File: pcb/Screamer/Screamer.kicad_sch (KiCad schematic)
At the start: 52 parts, among them J1 Conn_01x04, SW100 SW_DPDT_x2, SW102 SW_SPDT

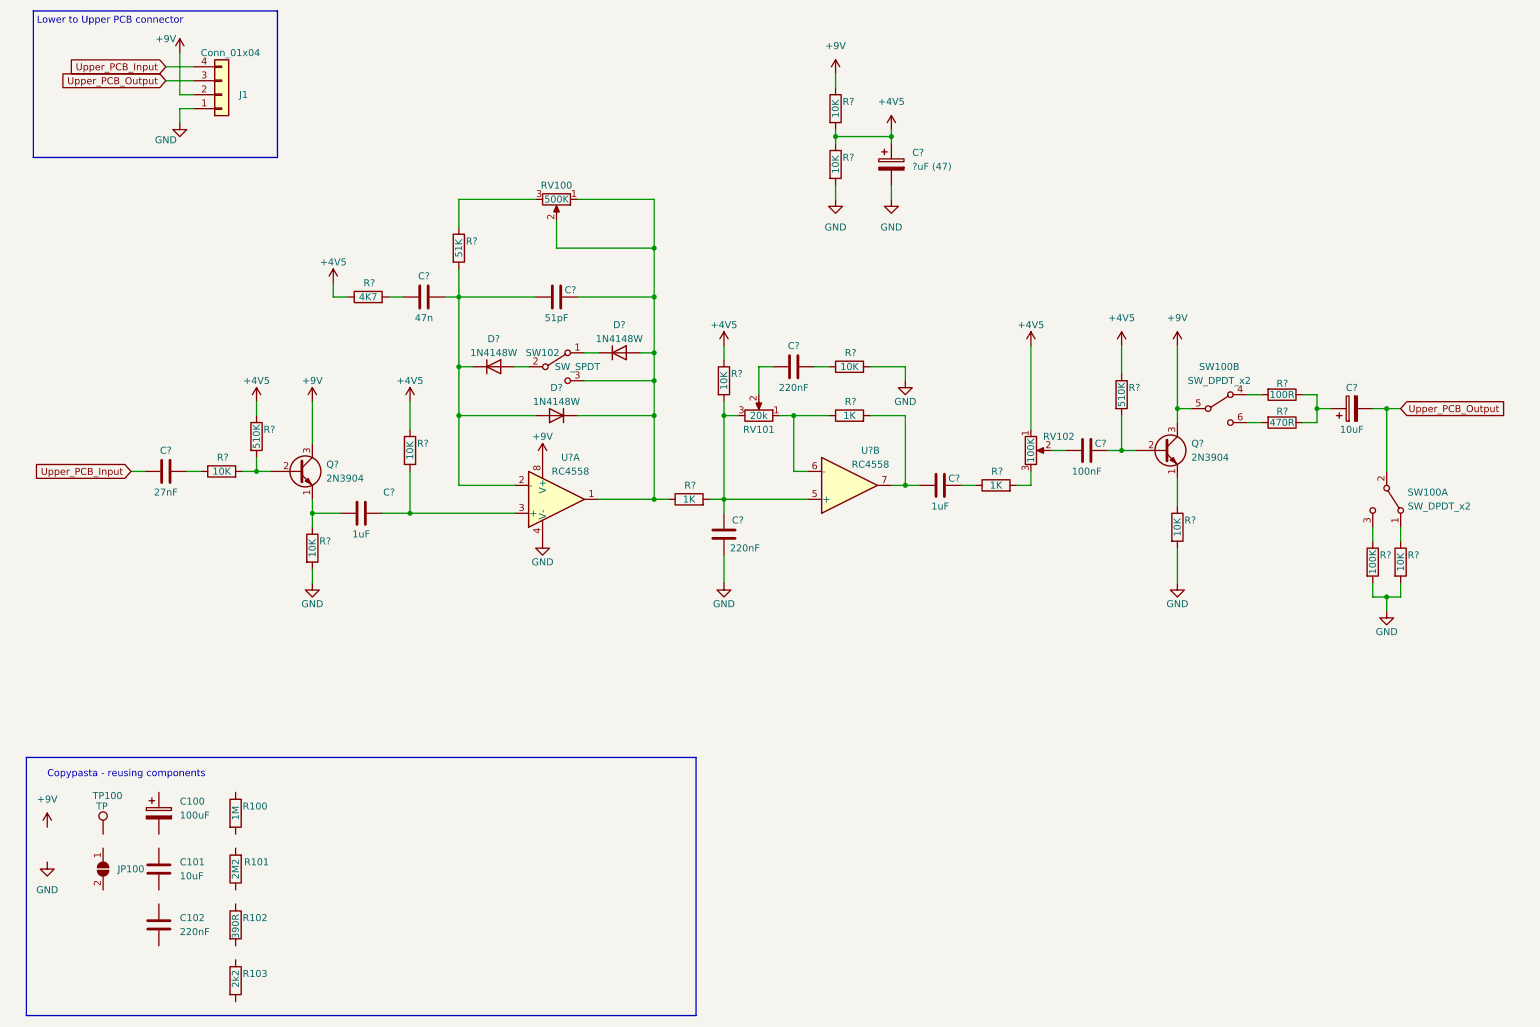
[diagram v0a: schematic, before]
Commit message: [Screamer] update schematic and assign LCSC parts
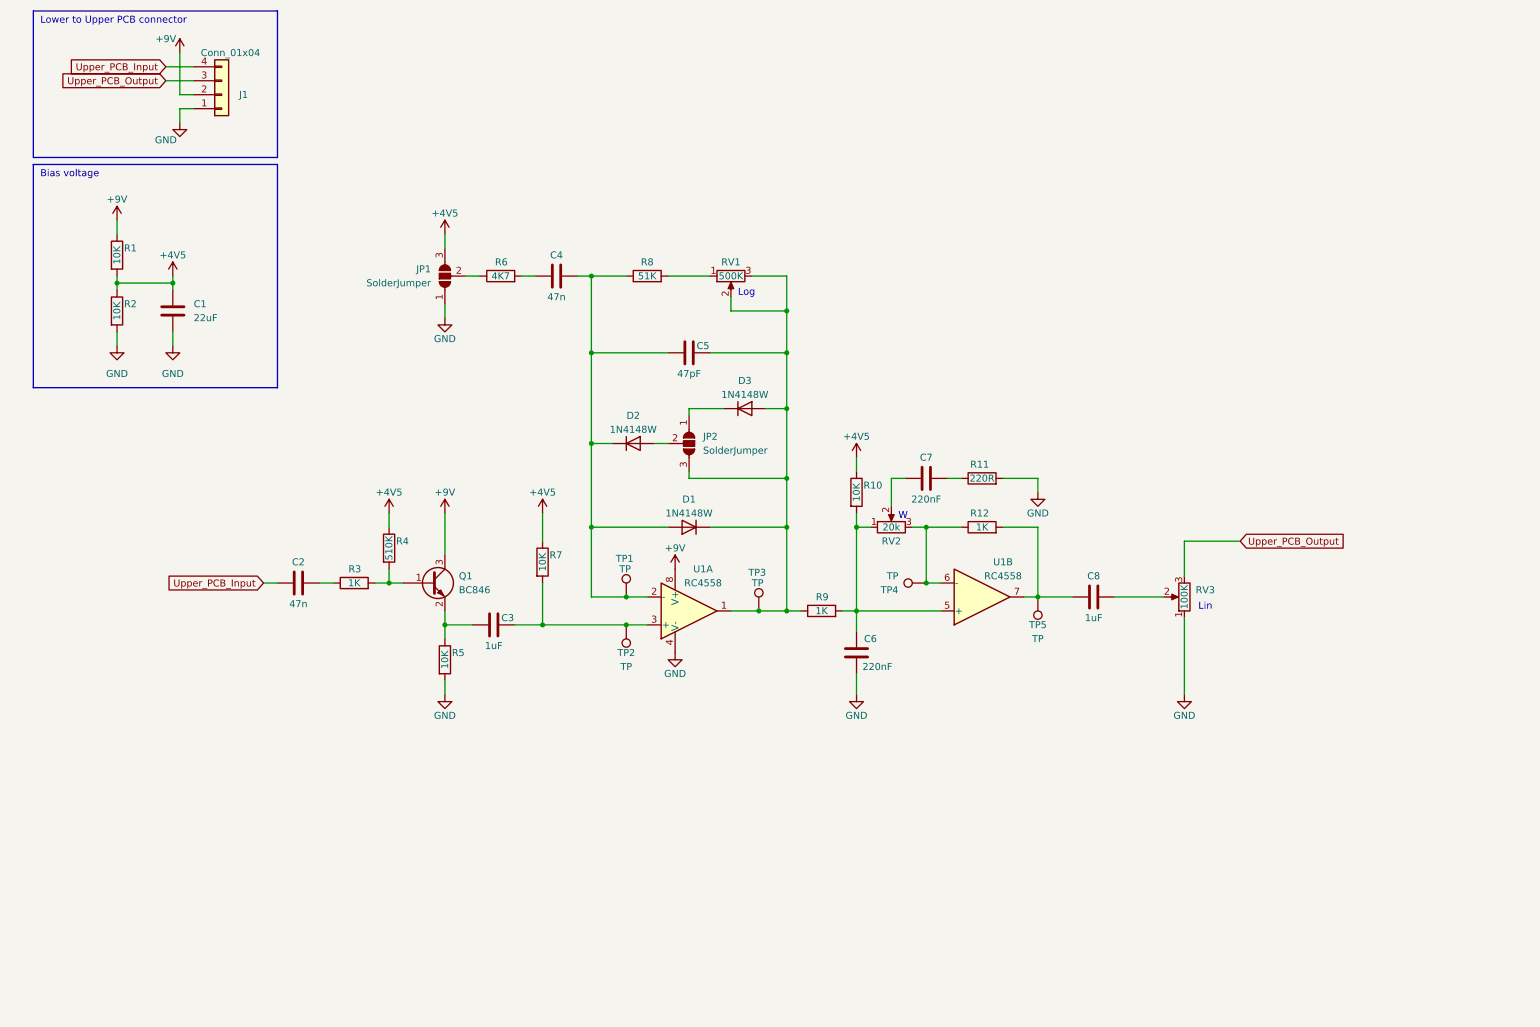
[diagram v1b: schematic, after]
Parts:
- removed C100: 100uF, Capacitor_THT:CP_Radial_D5.0mm_P2.00mm, symbol Device:C_Polarized
- removed C101: 10uF, Capacitor_SMD:C_0805_2012Metric, symbol Device:C
- removed C102: 220nF, Capacitor_SMD:C_0603_1608Metric, symbol Device:C
- removed C?: ?uF (47), symbol Device:C_Polarized
- removed C?: 10uF, symbol Device:C_Polarized
- removed C?: 100nF, symbol Device:C
- removed C?: 27nF, symbol Device:C
- removed JP100: Jmp, Jumper:SolderJumper-2_P1.3mm_Open_TrianglePad1.0x1.5mm, symbol Jumper:SolderJumper_2_Open
- removed Q? (x2): 2N3904, Package_TO_SOT_THT:TO-92_Inline, symbol Transistor_BJT:2N3904
- removed R100: 1M, Resistor_SMD:R_0603_1608Metric, symbol Device:R
- removed R101: 2M2, Resistor_SMD:R_0603_1608Metric, symbol Device:R
- removed R102: 390R, Resistor_SMD:R_0603_1608Metric, symbol Device:R
- removed R103: 2k2, Resistor_SMD:R_0603_1608Metric, symbol Device:R
- removed R?: 100K, Resistor_SMD:R_0603_1608Metric, symbol Device:R
- removed R? (x2): 10K, Resistor_SMD:R_0603_1608Metric, symbol Device:R
- removed R?: 510K, Resistor_SMD:R_0603_1608Metric, symbol Device:R
- removed R?: 470R, Resistor_SMD:R_0603_1608Metric, symbol Device:R
- removed R?: 1K, Resistor_SMD:R_0603_1608Metric, symbol Device:R
- removed R?: 100R, Resistor_SMD:R_0603_1608Metric, symbol Device:R
- removed SW100: SW_DPDT_x2, MeineBib:Switch_toggle_DPDT_Print, symbol Switch:SW_DPDT_x2
- removed SW102: SW_SPDT, MeineBib:Switch_toggle_SPDT_Print, symbol Switch:SW_SPDT
- removed TP100: TP, TestPoint:TestPoint_Pad_D2.0mm, symbol Connector:TestPoint
- added C1: 22uF, Capacitor_SMD:C_1206_3216Metric, symbol Device:C
- added C2: 47n, Capacitor_SMD:C_0603_1608Metric, symbol Device:C
- added JP1, JP2: SolderJumper, Jumper:SolderJumper-3_P1.3mm_Open_RoundedPad1.0x1.5mm_NumberLabels, symbol Jumper:SolderJumper_3_Open
- added Q1: BC846, Package_TO_SOT_SMD:SOT-23, symbol Transistor_BJT:BC846
- added TP1, TP2, TP3, TP4, TP5: TP, TestPoint:TestPoint_Pad_D2.0mm, symbol Connector:TestPoint
- C3, C8: renamed from C?; footprint (none) -> Capacitor_SMD:C_0603_1608Metric; LCSC C15850 -> C15849
- C4: renamed from C?; footprint (none) -> Capacitor_SMD:C_0603_1608Metric; LCSC C15850 -> C1622
- C5: renamed from C?; value 51pF -> 47pF; footprint (none) -> Capacitor_SMD:C_0603_1608Metric; LCSC C15850 -> C1671
- C6, C7: renamed from C?; footprint (none) -> Capacitor_SMD:C_0603_1608Metric; LCSC C15850 -> C21120
- R1, R10, R2, R5, R7: renamed from R?; LCSC (none) -> C25804
- R11: renamed from R?; value 10K -> 220R; LCSC (none) -> C22962
- R12, R9: renamed from R?; LCSC (none) -> C21190
- R3: renamed from R?; value 10K -> 1K; LCSC (none) -> C21190
- R4: renamed from R?; LCSC (none) -> C23192
- R6: renamed from R?; LCSC (none) -> C23162
- R8: renamed from R?; LCSC (none) -> C23196
- U1: renamed from U?; footprint (none) -> Package_SO:SO-8_3.9x4.9mm_P1.27mm; LCSC (none) -> C406864
- gave numbers to parts that had none: 3
- renumbered RV100 to RV1, RV101 to RV2, RV102 to RV3
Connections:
- net +9V: now also C1.1, JP1.3 (B), Q1.3 (C); no longer R6.1, RV3.1
- net GND: now also RV3.1, C1.2, JP1.1 (A)
- net Upper_PCB_Input: now also C2.1
- net Upper_PCB_Output: now also RV3.3
- net at C5.2, D1.1 (K), D3.2 (A)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: now also RV1.3, JP2.3 (B), TP3.1; no longer RV1.1
- net at C5.1, D1.2 (A), D2.1 (K)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: now also C4.1, R8.1, TP1.1; no longer C4.2, R8.2
- net at C3.1, R5.1: now also Q1.2 (E)
- net at R3.2, R4.2: now also Q1.1 (B)
- net at D3.1 (K): now also JP2.1 (A)
- net at D2.2 (A): now also JP2.2 (C)
- net at C6.1, R10.2, R9.2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: now also RV2.1; no longer RV2.3
- net at R6.2: now also C4.2; no longer C4.1
- net at C3.2, R7.2, U1.3 (+): now also TP2.1
- net at R3.1: now also C2.2
- net at R12.1, U1.6 (-): now also RV2.3, TP4.1; no longer RV2.1
- net at C8.1, R12.2, U1.7: now also TP5.1
- net at C8.2: now also RV3.2
- new net: R8.2, RV1.1
- new net: JP1.2 (C), R6.1
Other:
- note added: "Bias voltage"
- note added: "Lin"
- note added: "Log"
- note added: "W"
- note removed: "Copypasta - reusing components"
- moved on the sheet: C3, C4, C5, C6, C7, C8, D1, D2, D3, R1, R10, R11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

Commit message: [Screamer] Update diode footprint and start arranging stuff on PCB
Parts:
- D1, D2, D3: footprint Diode_SMD:D_SOD-123 -> MeineBib:D_SOD-123+THT
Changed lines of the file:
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@@
     (property "Reference" "D1" (id 0) (at 133.35 102.87 0))
     (property "Value" "1N4148W" (id 1) (at 133.35 105.41 0))
-    (property "Footprint" "Diode_SMD:D_SOD-123" (id 2) (at 133.35 103.505 0)
+    (property "Footprint" "MeineBib:D_SOD-123+THT" (id 2) (at 133.35 103.505 0)
       (effects (font (size 1.27 1.27)) hide)
     )
@@
     (property "Reference" "D3" (id 0) (at 143.51 81.28 0))
     (property "Value" "1N4148W" (id 1) (at 143.51 83.82 0))
-    (property "Footprint" "Diode_SMD:D_SOD-123" (id 2) (at 143.51 90.805 0)
+    (property "Footprint" "MeineBib:D_SOD-123+THT" (id 2) (at 143.51 90.805 0)
       (effects (font (size 1.27 1.27)) hide)
     )
@@
     (property "Reference" "D2" (id 0) (at 123.19 87.63 0))
     (property "Value" "1N4148W" (id 1) (at 123.19 90.17 0))
-    (property "Footprint" "Diode_SMD:D_SOD-123" (id 2) (at 123.19 97.155 0)
+    (property "Footprint" "MeineBib:D_SOD-123+THT" (id 2) (at 123.19 97.155 0)
       (effects (font (size 1.27 1.27)) hide)
     )
@@
     )
     (path "/06bd8af6-5f31-48d1-8dfe-e47bb2fbf937"
-      (reference "D1") (unit 1) (value "1N4148W") (footprint "Diode_SMD:D_SOD-123")
+      (reference "D1") (unit 1) (value "1N4148W") (footprint "MeineBib:D_SOD-123+THT")
     )
     (path "/8885a9d9-16dd-4476-9879-de777ac2f14c"
-      (reference "D2") (unit 1) (value "1N4148W") (footprint "Diode_SMD:D_SOD-123")
+      (reference "D2") (unit 1) (value "1N4148W") (footprint "MeineBib:D_SOD-123+THT")
     )
     (path "/2b9560aa-ca85-40bd-96c0-e06c0c8c5ac1"
-      (reference "D3") (unit 1) (value "1N4148W") (footprint "Diode_SMD:D_SOD-123")
+      (reference "D3") (unit 1) (value "1N4148W") (footprint "MeineBib:D_SOD-123+THT")
     )
     (path "/43624bd7-5b28-4455-bedf-a59e39f0128d"

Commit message: [Screamer] Initially route Screamer PCB
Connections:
- net +9V: no longer C1.1, JP1.3 (B), R1.2, R10.1, R2.1, R4.1, R7.1
- net at C5.2, D1.1 (K), D3.2 (A)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: now also R8.1; no longer RV1.2, RV1.3
- net at C4.1, C5.1, D1.2 (A)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: now also RV1.1; no longer R8.1
- net at R8.2: now also RV1.2, RV1.3; no longer RV1.1
- new net +4V5: C1.1, JP1.3 (B), R1.2, R10.1, R2.1, R4.1, R7.1
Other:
- moved on the sheet: R8, RV1
